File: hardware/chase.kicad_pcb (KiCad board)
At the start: 2 copper layers, 52 x 52 mm, 181 parts, among them J1 THD0509-04CL-GF, Q1 DMC3400SDW-7, Q2 DMN61D9UDW, Q3 DMN61D9UDW, SW1 TS-1187A-B-A-B, T1 TestPoint, T2 TestPoint, T3 TestPoint, T4 TestPoint, T5 TestPoint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

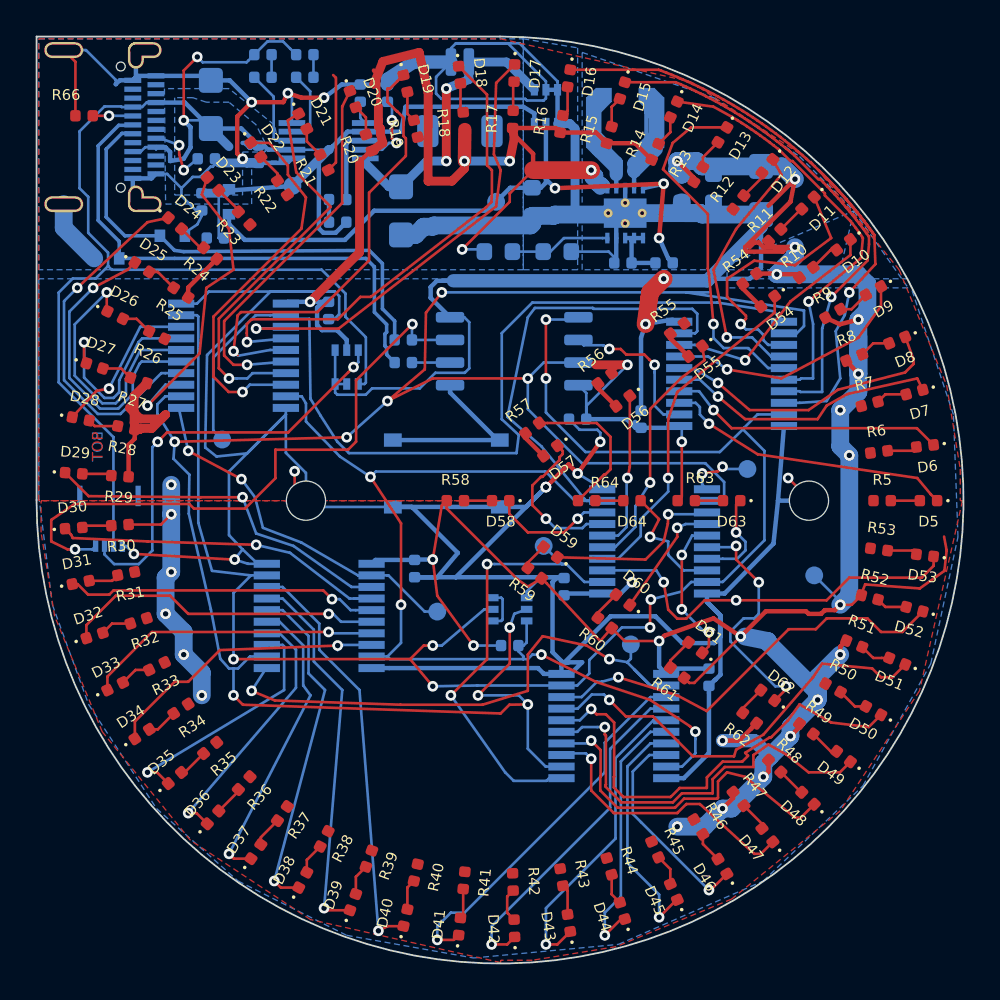
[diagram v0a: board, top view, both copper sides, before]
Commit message: Replace J1 with 6 pin connector, use cheaper resistor for 430 ohms.
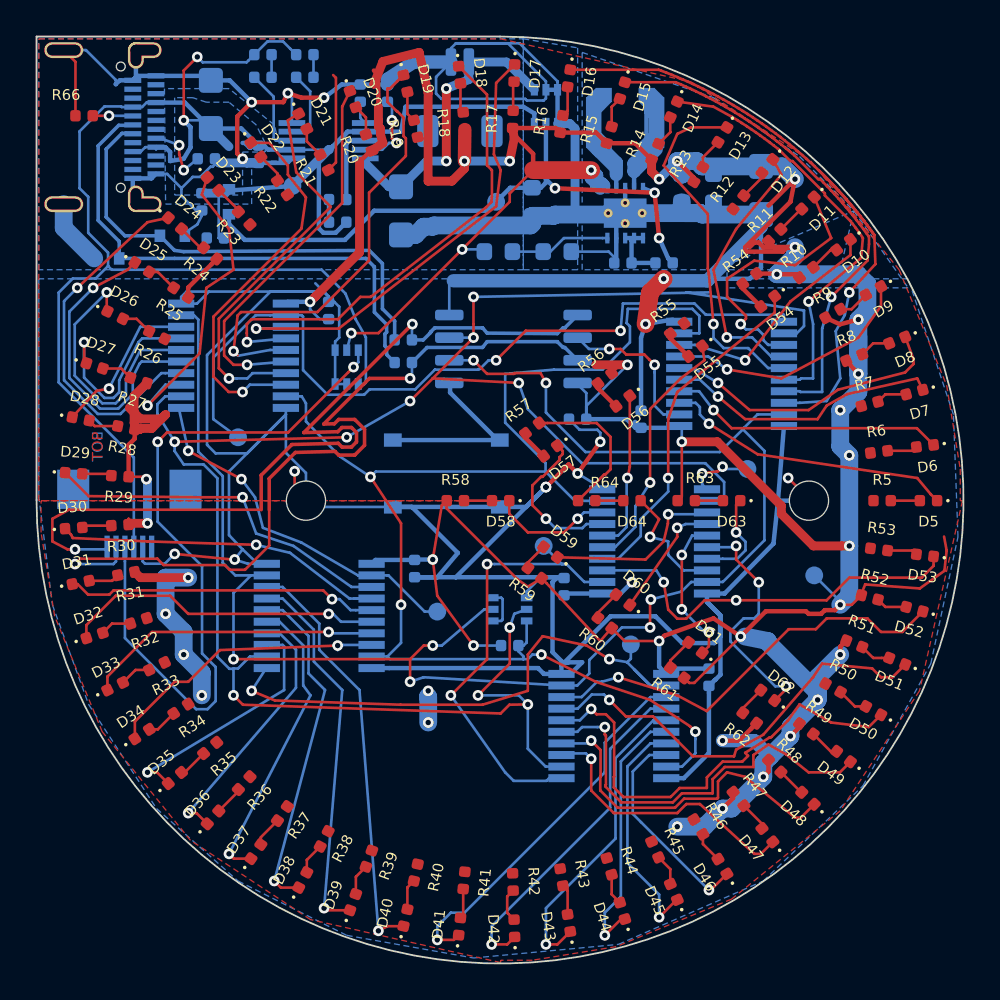
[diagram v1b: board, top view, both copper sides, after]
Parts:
- J1: value THD0509-04CL-GF -> FH12-6S-0.5SH(55); footprint chase-libs:THD050904CLGF -> Connector_FFC-FPC:Hirose_FH12-6S-0.5SH_1x06-1MP_P0.50mm_Horizontal
- moved J1 1.17 mm to (106.0, 127.5)
- moved T1 0.90 mm to (112.1, 123.2)
- moved U1 0.13 mm to (127.5, 118.3)
- turned C10 to 270 degrees
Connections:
- J1 pad 2: XVCC -> D+
- J1 pad 3: VBUS -> XVCC
- J1 pad 4: GND -> VBUS
- J1 pad 5: (no net) -> GND
- J1 pad 6: (no net) -> Net-(J1-Pad6)
- U1 pad 2: D+ -> /LED Driver 1/SRCK
- U1 pad 3: D- -> /LED Driver 1/RCK
- U1 pad 5: /LED Driver 1/SRCK -> D-
- U1 pad 7: /LED Driver 1/RCK -> D+
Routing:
- net D+: track 2.14 -> 45.6 mm, vias 0 -> 2
- net VCC: track 306.2 -> 329.3 mm, vias 34 -> 39
- net XVCC: track 23.7 -> 41.7 mm
- net D-: track 34.9 -> 47.9 mm
- net GND: track 342.9 -> 332.1 mm
- net /LED Driver 2/SER_IN: track 52.9 -> 45.3 mm, vias 0 -> 2
- net /LED Driver 1/RCK: track 123.8 -> 118.8 mm, vias 9 -> 10
- net /LED Driver 1/~CLR: track 82.2 -> 79.5 mm
- net VBATOUT: track 36.0 -> 34.5 mm
- net /LED Driver 1/SRCK: track 93.5 -> 94.3 mm
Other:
- board text added: "2 XSIG2"
- board text added: "3 XVCC"
- board text added: "4 EN_"
- board text added: "5 GND"
- board text added: "6 NC"
- board text added: "chase-rev9"
- board text removed: "2 XVCC"
- board text removed: "3 EN_"
- board text removed: "4 GND"
- board text removed: "chase-r8"

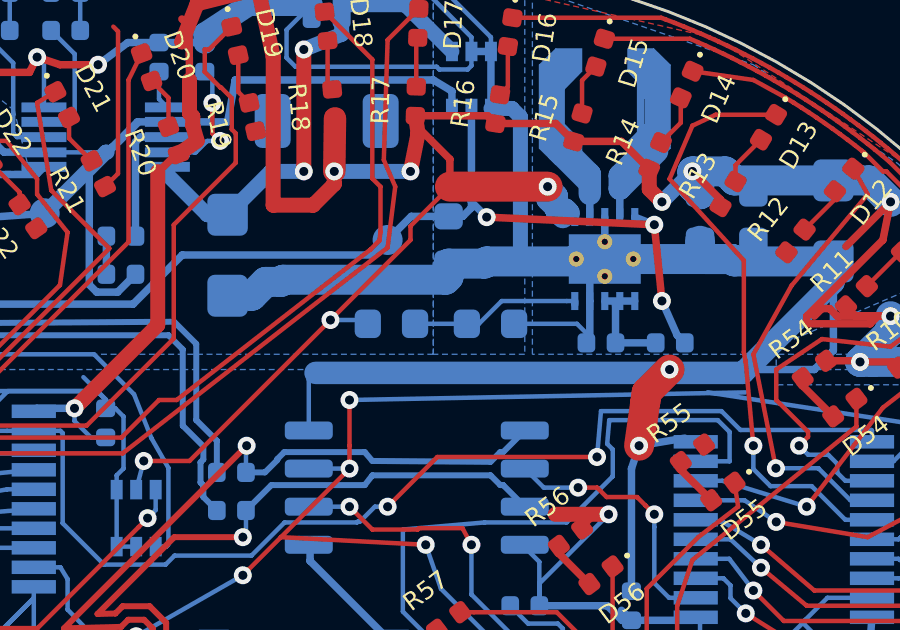
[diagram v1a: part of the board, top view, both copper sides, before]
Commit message: Change TPS63000 variable to TPS63001 3.3V buck-boost.
TPS630001 is in stock now, can use it again. R73 and R74 are not
necessary now.

Change resistor brand for 71.5ohm resistors.

From VikingTech to UniRoyal which is cheaper.
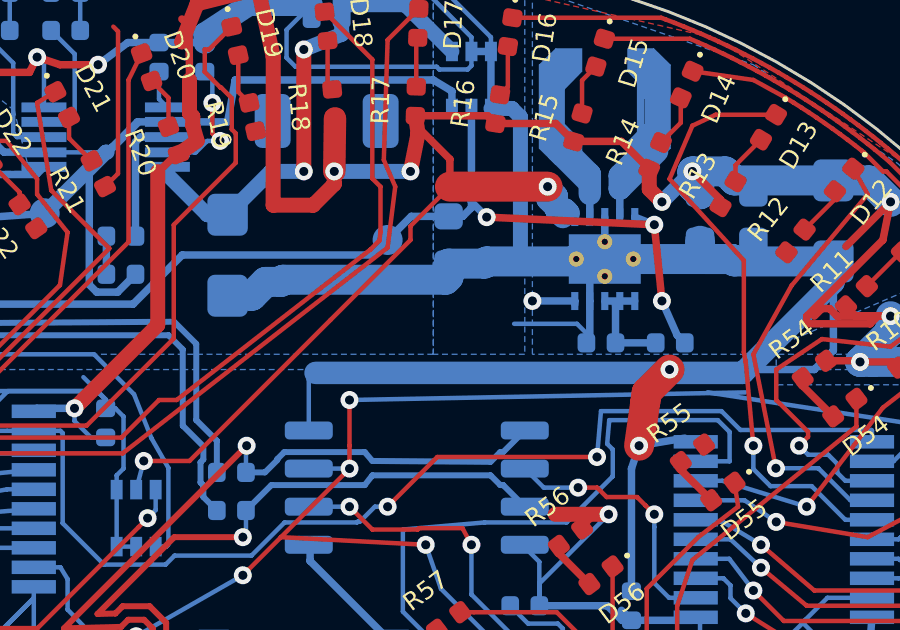
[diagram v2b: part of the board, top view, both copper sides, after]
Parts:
- removed R73: 1M, Resistor_SMD:R_0603_1608Metric
- removed R74: 178K, Resistor_SMD:R_0603_1608Metric
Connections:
- U2 pad 10: Net-(R73-Pad1) -> VCC
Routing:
- net Net-(R73-Pad1): track 5.75 -> 0.00 mm
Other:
- board text added: "chase-rev10"
- board text removed: "chase-rev9"
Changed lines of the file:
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@@
     (thickness 1.6)
     (drawings 12)
-    (tracks 2030)
+    (tracks 2025)
     (zones 0)
-    (modules 181)
-    (nets 169)
+    (modules 179)
+    (nets 168)
   )
   (page A4)
@@
       (drillshape 0)
       (scaleselection 1)
-      (outputdirectory "fabrication/rev-9/"))
+      (outputdirectory "fabrication/rev-10/"))
   )
   (net 0 "")
@@
   (net 165 "Net-(R72-Pad1)")
   (net 166 XVCC)
-  (net 167 "Net-(R73-Pad1)")
-  (net 168 "Net-(J1-Pad6)")
+  (net 167 "Net-(J1-Pad6)")
   (net_class Default "This is the default net class."
     (clearance 0.15)
@@
     (add_net "Net-(R71-Pad1)")
     (add_net "Net-(R72-Pad1)")
-    (add_net "Net-(R73-Pad1)")
     (add_net "Net-(RT2-Pad2)")
     (add_net "Net-(SW1-PadC1)")
@@
     (fp_line (start 0 1.2) (end -3.05 1.2) (layer B.Fab) (width 0.1))
     (pad 6 smd rect (at 1.25 1.85) (size 0.3 1.3) (layers B.Cu B.Paste B.Mask)
-      (net 168 "Net-(J1-Pad6)"))
+      (net 167 "Net-(J1-Pad6)"))
     (pad 5 smd rect (at 0.75 1.85) (size 0.3 1.3) (layers B.Cu B.Paste B.Mask)
       (net 2 GND))
@@
     )
   )
-  (module Resistor_SMD:R_0603_1608Metric (layer B.Cu)
-    (at 129.96 112.815 180)
-    (descr "Resistor SMD 0603 (1608 Metric), square (rectangular) end terminal, IPC_7351 nominal, (Body size source: http://www.tortai-tech.com/upload/download/2011102023233369053.pdf), generated with kicad-footprint-generator")
-    (tags resistor)
-    (attr smd)
-    (fp_text reference R74 (at 0 1.43) (layer B.SilkS)
-      (effects (font (size 0.6 0.6) (thickness 0.15)) (justify mirror))
-    )
-    (fp_text value 178K (at 0 -1.43) (layer B.Fab)
-      (effects (font (size 1 1) (thickness 0.15)) (justify mirror))
-    )
-    (fp_text user %R (at 0 0) (layer B.Fab)
-      (effects (font (size 0.4 0.4) (thickness 0.06)) (justify mirror))
-    )
-    (fp_line (start 1.48 -0.73) (end -1.48 -0.73) (layer B.CrtYd) (width 0.05))
-    (fp_line (start 1.48 0.73) (end 1.48 -0.73) (layer B.CrtYd) (width 0.05))
-    (fp_line (start -1.48 0.73) (end 1.48 0.73) (layer B.CrtYd) (width 0.05))
-    (fp_line (start -1.48 -0.73) (end -1.48 0.73) (layer B.CrtYd) (width 0.05))
-    (fp_line (start -0.162779 -0.51) (end 0.162779 -0.51) (layer B.SilkS) (width 0.12))
-    (fp_line (start -0.162779 0.51) (end 0.162779 0.51) (layer B.SilkS) (width 0.12))
-    (fp_line (start 0.8 -0.4) (end -0.8 -0.4) (layer B.Fab) (width 0.1))
-    (fp_line (start 0.8 0.4) (end 0.8 -0.4) (layer B.Fab) (width 0.1))
-    (fp_line (start -0.8 0.4) (end 0.8 0.4) (layer B.Fab) (width 0.1))
-    (fp_line (start -0.8 -0.4) (end -0.8 0.4) (layer B.Fab) (width 0.1))
-    (pad 2 smd roundrect (at 0.7875 0 180) (size 0.875 0.95) (layers B.Cu B.Paste B.Mask) (roundrect_rratio 0.25)
-      (net 167 "Net-(R73-Pad1)"))
-    (pad 1 smd roundrect (at -0.7875 0 180) (size 0.875 0.95) (layers B.Cu B.Paste B.Mask) (roundrect_rratio 0.25)
-      (net 2 GND))
-    (model ${KISYS3DMOD}/Resistor_SMD.3dshapes/R_0603_1608Metric.wrl
-      (at (xyz 0 0 0))
-      (scale (xyz 1 1 1))
-      (rotate (xyz 0 0 0))
-    )
-  )
-  (module Resistor_SMD:R_0603_1608Metric (layer B.Cu)
-    (at 126.658 112.815 180)
-    (descr "Resistor SMD 0603 (1608 Metric), square (rectangular) end terminal, IPC_7351 nominal, (Body size source: http://www.tortai-tech.com/upload/download/2011102023233369053.pdf), generated with kicad-footprint-generator")
-    (tags resistor)
-    (attr smd)
-    (fp_text reference R73 (at 2.413 -0.635) (layer B.SilkS)
-      (effects (font (size 0.6 0.6) (thickness 0.15)) (justify mirror))
-    )
-    (fp_text value 1M (at 0 -1.43) (layer B.Fab)
-      (effects (font (size 1 1) (thickness 0.15)) (justify mirror))
-    )
-    (fp_text user %R (at 0 0) (layer B.Fab)
-      (effects (font (size 0.4 0.4) (thickness 0.06)) (justify mirror))
-    )
-    (fp_line (start 1.48 -0.73) (end -1.48 -0.73) (layer B.CrtYd) (width 0.05))
-    (fp_line (start 1.48 0.73) (end 1.48 -0.73) (layer B.CrtYd) (width 0.05))
-    (fp_line (start -1.48 0.73) (end 1.48 0.73) (layer B.CrtYd) (width 0.05))
-    (fp_line (start -1.48 -0.73) (end -1.48 0.73) (layer B.CrtYd) (width 0.05))
-    (fp_line (start -0.162779 -0.51) (end 0.162779 -0.51) (layer B.SilkS) (width 0.12))
-    (fp_line (start -0.162779 0.51) (end 0.162779 0.51) (layer B.SilkS) (width 0.12))
-    (fp_line (start 0.8 -0.4) (end -0.8 -0.4) (layer B.Fab) (width 0.1))
-    (fp_line (start 0.8 0.4) (end 0.8 -0.4) (layer B.Fab) (width 0.1))
-    (fp_line (start -0.8 0.4) (end 0.8 0.4) (layer B.Fab) (width 0.1))
-    (fp_line (start -0.8 -0.4) (end -0.8 0.4) (layer B.Fab) (width 0.1))
-    (pad 2 smd roundrect (at 0.7875 0 180) (size 0.875 0.95) (layers B.Cu B.Paste B.Mask) (roundrect_rratio 0.25)
-      (net 1 VCC))
-    (pad 1 smd roundrect (at -0.7875 0 180) (size 0.875 0.95) (layers B.Cu B.Paste B.Mask) (roundrect_rratio 0.25)
-      (net 167 "Net-(R73-Pad1)"))
-    (model ${KISYS3DMOD}/Resistor_SMD.3dshapes/R_0603_1608Metric.wrl
-      (at (xyz 0 0 0))
-      (scale (xyz 1 1 1))
-      (rotate (xyz 0 0 0))
-    )
-  )
   (module Package_TO_SOT_SMD:SOT-363_SC-70-6 (layer B.Cu)
     (at 129.325 104.687 90)
@@
       ))
     (pad 10 smd rect (at 1.4 1 270) (size 0.6 0.24) (layers B.Cu B.Paste B.Mask)
-      (net 167 "Net-(R73-Pad1)"))
+      (net 1 VCC))
     (pad 9 smd rect (at 1.4 0.5 270) (size 0.6 0.24) (layers B.Cu B.Paste B.Mask)
       (net 2 GND))
@@
     (effects (font (size 0.6 0.6) (thickness 0.15)) (justify mirror))
   )
-  (gr_text chase-rev9 (at 124.372 143.676) (layer B.SilkS)
+  (gr_text chase-rev10 (at 124.372 143.676) (layer B.SilkS)
     (effects (font (size 0.6 0.6) (thickness 0.13)) (justify mirror))
   )
@@
   (segment (start 136.691 108.243) (end 136.691 107.735) (width 1) (layer B.Cu) (net 1))
   (segment (start 136.945 108.497) (end 136.691 108.243) (width 1) (layer B.Cu) (net 1))
-  (via (at 124.626 112.688) (size 0.6) (drill 0.3) (layers F.Cu B.Cu) (net 1))
-  (segment (start 125.7435 112.688) (end 125.8705 112.815) (width 0.15) (layer B.Cu) (net 1))
-  (segment (start 124.626 112.688) (end 125.7435 112.688) (width 0.15) (layer B.Cu) (net 1))
   (segment (start 127.293 109.556998) (end 128.606998 108.243) (width 0.15) (layer F.Cu) (net 1))
   (segment (start 127.293 110.021) (end 127.293 109.556998) (width 0.15) (layer F.Cu) (net 1))
@@
   (via (at 118.403 117.387) (size 0.6) (drill 0.3) (layers F.Cu B.Cu) (net 1))
   (segment (start 118.403 117.387) (end 118.149 118.342) (width 0.15) (layer B.Cu) (net 1))
+  (segment (start 132.77 112.056) (end 132.77 112.164) (width 0.25) (layer B.Cu) (net 1))
+  (via (at 131.357 112.053) (size 0.6) (drill 0.3) (layers F.Cu B.Cu) (net 1))
+  (segment (start 132.767 112.053) (end 132.77 112.056) (width 0.25) (layer B.Cu) (net 1))
+  (segment (start 131.357 112.053) (end 132.767 112.053) (width 0.25) (layer B.Cu) (net 1))
   (via (at 112.307 107.608) (size 0.6) (drill 0.3) (layers F.Cu B.Cu) (net 2))
   (via (at 114.847 103.925) (size 0.6) (drill 0.3) (layers F.Cu B.Cu) (net 2))
@@
   (segment (start 107.5445 127.965998) (end 110.03401 130.455508) (width 0.15) (layer B.Cu) (net 166))
   (segment (start 107.5445 123.483) (end 107.5445 127.965998) (width 0.15) (layer B.Cu) (net 166))
-  (segment (start 132.77 112.056) (end 132.77 112.164) (width 0.25) (layer B.Cu) (net 167))
-  (segment (start 127.4455 112.815) (end 129.1725 112.815) (width 0.15) (layer B.Cu) (net 167))
-  (segment (start 132.5 112.056) (end 132.77 112.056) (width 0.15) (layer B.Cu) (net 167))
-  (segment (start 129.574216 112.815) (end 130.333216 112.056) (width 0.15) (layer B.Cu) (net 167))
-  (segment (start 130.333216 112.056) (end 132.5 112.056) (width 0.15) (layer B.Cu) (net 167))
-  (segment (start 129.1725 112.815) (end 129.574216 112.815) (width 0.15) (layer B.Cu) (net 167))
   (zone (net 1) (net_name VCC) (layer F.Cu) (hatch edge 0.508)
     (connect_pads (clearance 0.508))
